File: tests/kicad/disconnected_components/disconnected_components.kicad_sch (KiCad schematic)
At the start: 3 parts

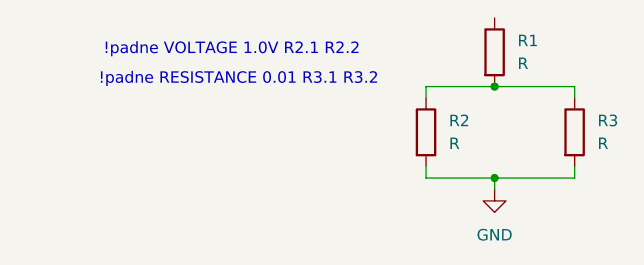
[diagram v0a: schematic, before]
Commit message: feat: Richer directive syntax
This commit adds support for named directive parameters. No more
guessing which parameter is the positive terminal positive and which is the
negative terminal!
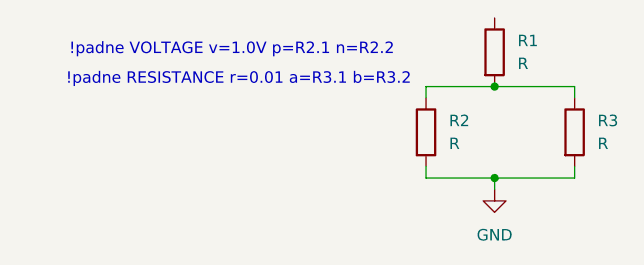
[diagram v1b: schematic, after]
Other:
- note added: "!padne RESISTANCE r=0.01 a=R3.1 b=R3.2"
- note added: "!padne VOLTAGE v=1.0V p=R2.1 n=R2.2"
- note removed: "!padne RESISTANCE 0.01 R3.1 R3.2"
- note removed: "!padne VOLTAGE 1.0V R2.1 R2.2"
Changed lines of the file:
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@@
 		)
 	)
-	(text "!padne VOLTAGE 1.0V R2.1 R2.2"
+	(text "!padne VOLTAGE v=1.0V p=R2.1 n=R2.2"
 		(exclude_from_sim no)
 		(at 118.11 96.266 0)
@@
 		)
 	)
-	(text "!padne RESISTANCE 0.01 R3.1 R3.2"
+	(text "!padne RESISTANCE r=0.01 a=R3.1 b=R3.2"
 		(exclude_from_sim no)
 		(at 118.872 99.568 0)
